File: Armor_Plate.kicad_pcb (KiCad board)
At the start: 2 copper layers, 120 x 117 mm, 47 parts, among them SW3 SW_SP3T

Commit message: Updated fab files
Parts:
- removed ?: , 
- BT1: footprint Battery:BatteryHolder_Keystone_2468_2xAAA -> Battery:BatteryHolder_Keystone_2466_1xAAA
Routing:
- net /3V blue: track 0.00 -> 212.8 mm, vias 0 -> 2
- net /3V Red: track 95.0 -> 249.9 mm, vias 0 -> 2
- net Net-(BT1-+): track 0.00 -> 36.4 mm

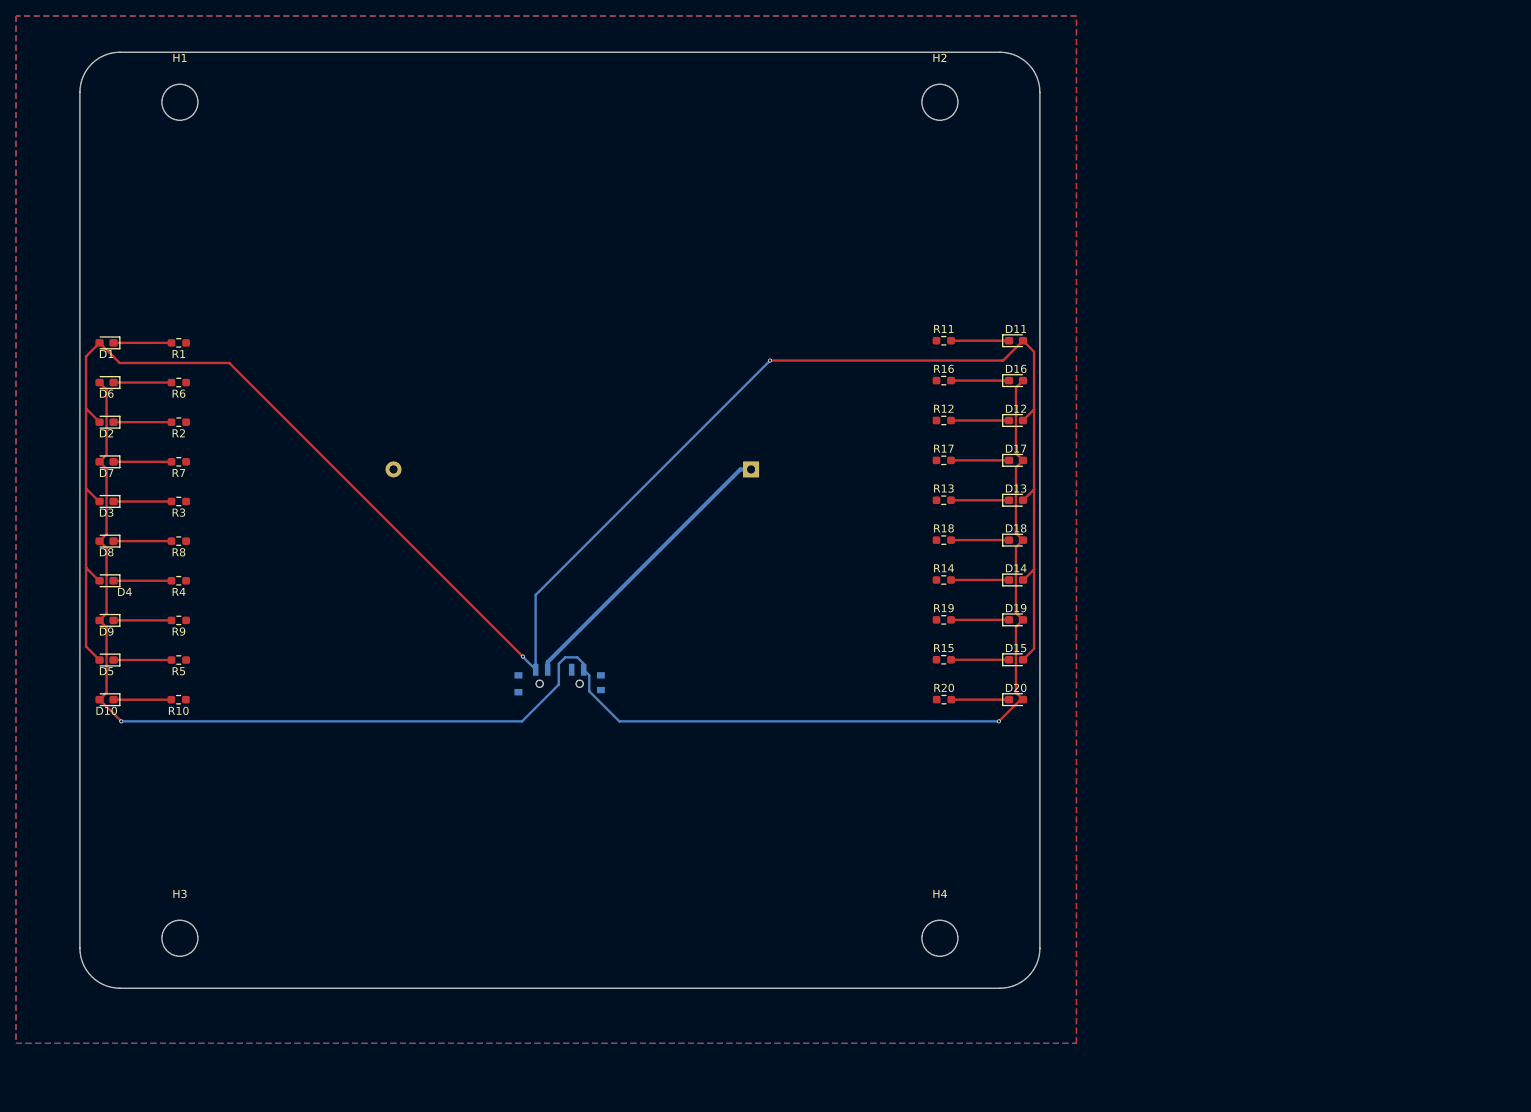
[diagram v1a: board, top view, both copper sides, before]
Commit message: Updated Armor Plate 2 batteries
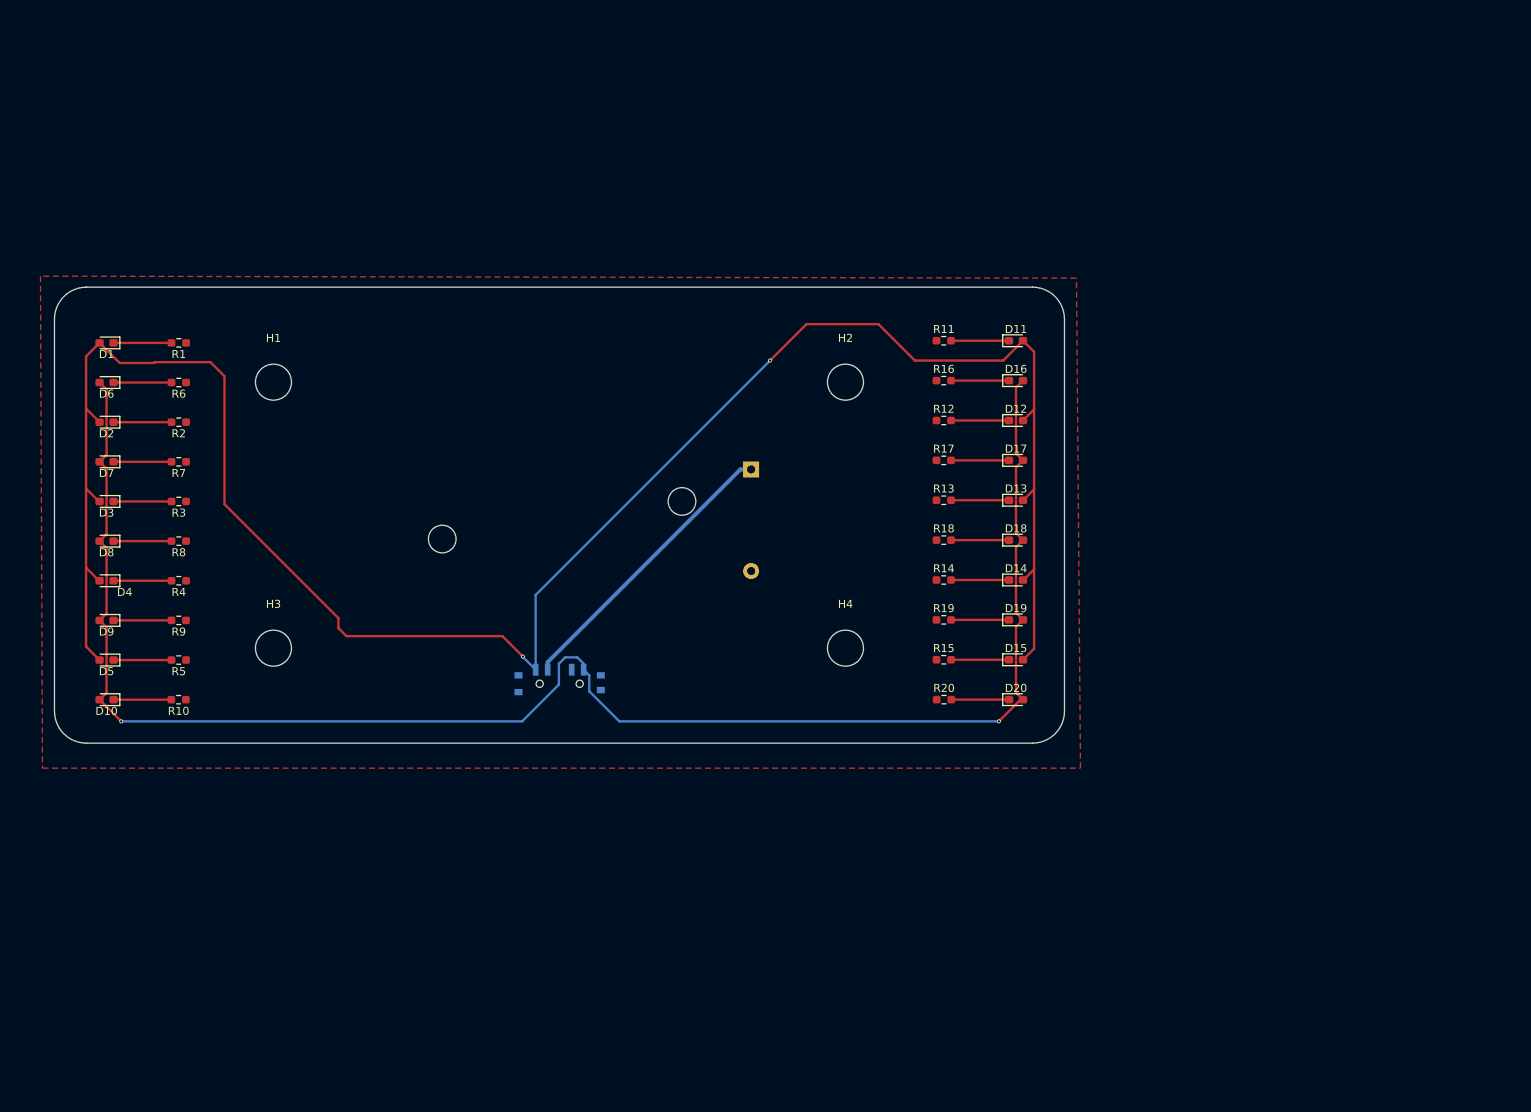
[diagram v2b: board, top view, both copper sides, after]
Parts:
- BT1: footprint Battery:BatteryHolder_Keystone_2466_1xAAA -> Battery:BatteryHolder_Keystone_2468_2xAAA
- moved H4 38.1 mm to (115.6, 91.0)
- moved H3 38.1 mm to (44.1, 91.0)
- moved H2 36.9 mm to (115.6, 57.7)
- moved H1 36.9 mm to (44.1, 57.7)
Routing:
- net /3V Red: track 249.9 -> 263.9 mm
- removed copper zone on B.Cu, net GND
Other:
- board size 120 x 117 mm -> 126.3 x 57 mm

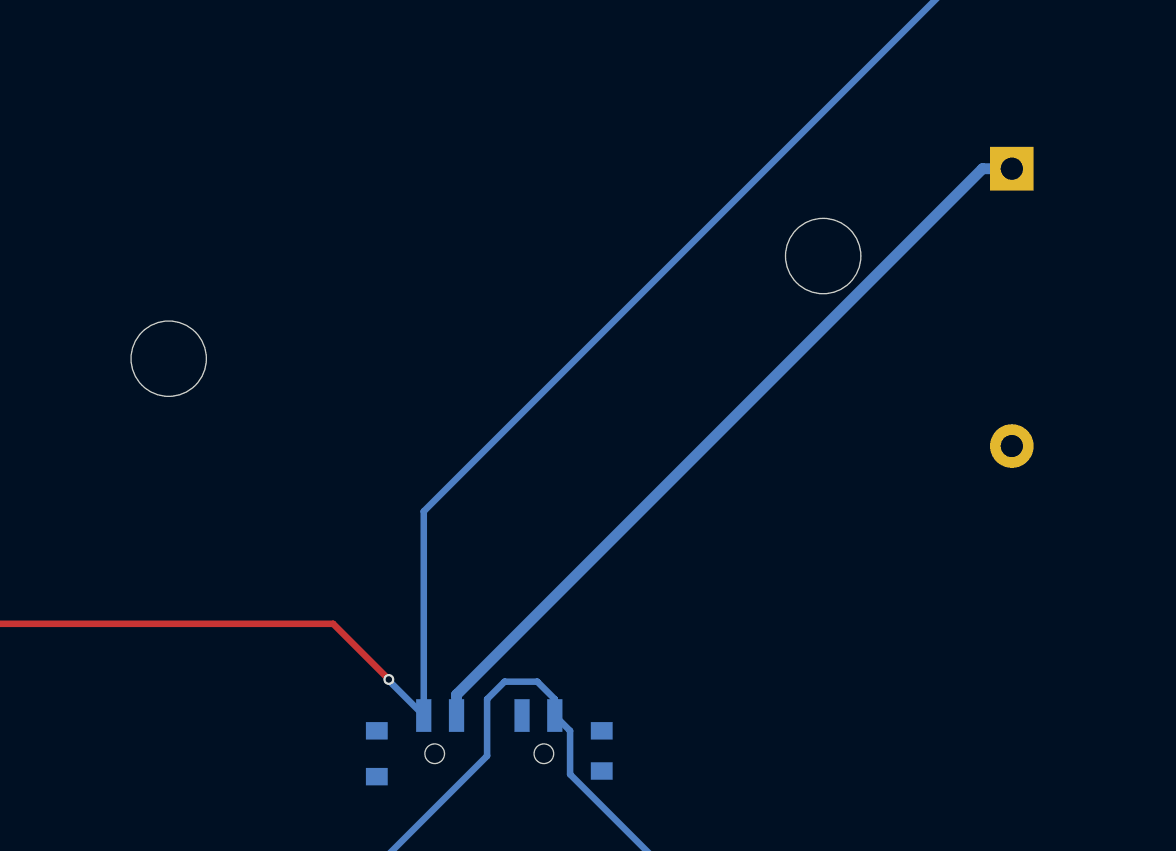
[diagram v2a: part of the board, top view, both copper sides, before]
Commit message: Changed battery cell footprint to hold 3 batteries
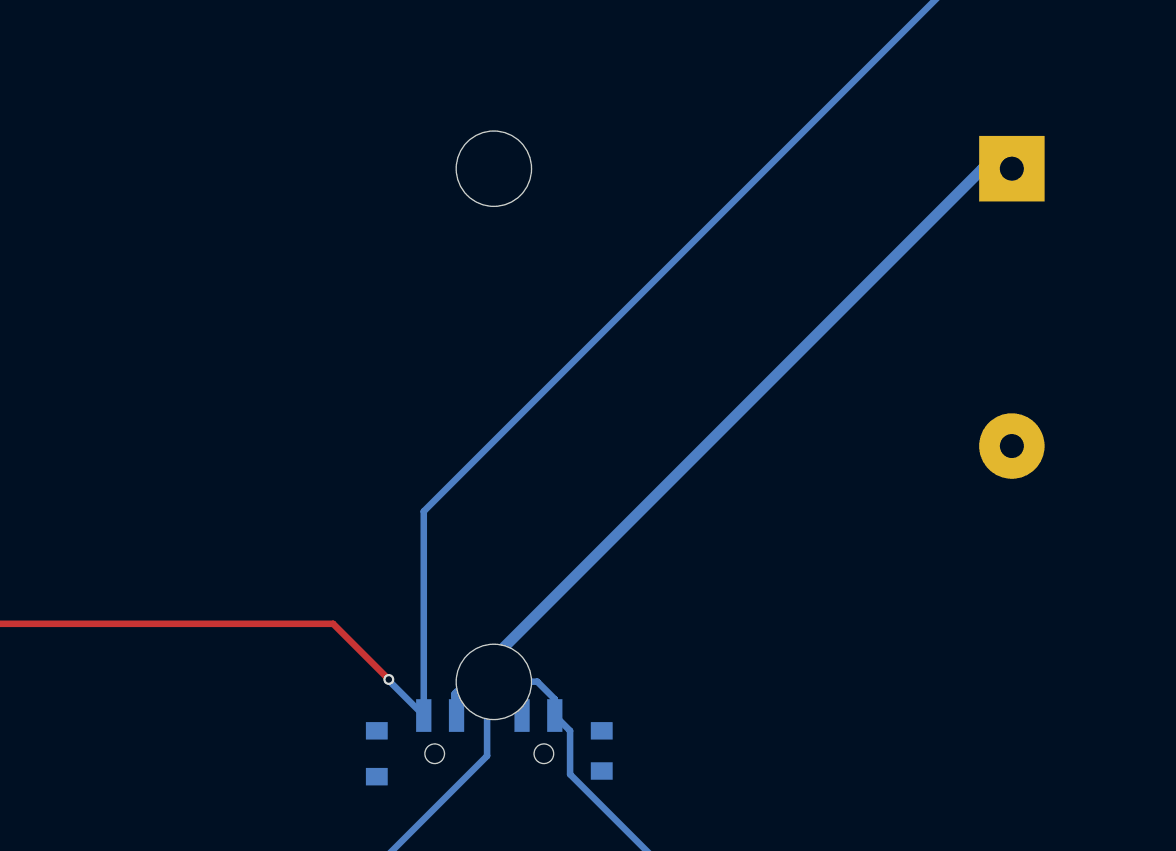
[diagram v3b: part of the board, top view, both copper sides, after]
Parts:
- BT1: footprint Battery:BatteryHolder_Keystone_2468_2xAAA -> Battery:BatteryHolder_Keystone_2479_3xAAA
